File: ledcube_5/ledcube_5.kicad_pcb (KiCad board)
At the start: 2 copper layers, 60 parts, among them J1 Conn_01x05_MountingPin, Q1 PN2222A, Q2 PN2222A, Q3 PN2222A, Q4 PN2222A, Q5 PN2222A, U1 74HC595, U2 74HC595, U3 74HC595, U4 74HC595

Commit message: ledcube pcb tracks
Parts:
- added J2: Conn_01x01, Connector_Pin:Pin_D1.0mm_L10.0mm, F.Cu at (241.3, 102.9)
- added J3: Conn_01x01, Connector_Pin:Pin_D1.0mm_L10.0mm, F.Cu at (241.3, 106.9)
- added J4: Conn_01x01, Connector_Pin:Pin_D1.0mm_L10.0mm, F.Cu at (245.3, 102.9)
- added J5: Conn_01x01, Connector_Pin:Pin_D1.0mm_L10.0mm, F.Cu at (245.3, 106.9)
- added J6: Conn_01x01, Connector_Pin:Pin_D1.0mm_L10.0mm, F.Cu at (249.4, 102.9)
- J1: footprint Connector_PinHeader_1.00mm:PinHeader_1x05_P1.00mm_Vertical -> Connector_PinHeader_2.54mm:PinHeader_1x05_P2.54mm_Vertical
- moved J1 2.34 mm to (248.7, 82.0)
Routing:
- net GND: track 0.00 -> 231.7 mm
- net +5V: track 0.00 -> 210.6 mm
- net /U3_F: track 0.00 -> 104.6 mm
- net /A0: track 0.00 -> 84.8 mm
- net /A4: track 0.00 -> 84.6 mm
- net /U3_G: track 0.00 -> 80.7 mm
- net /U3_H: track 0.00 -> 69.0 mm
- net /U4_B: track 0.00 -> 67.1 mm
- net Net-(J6-Pad1): track 0.00 -> 58.3 mm
- net /U2_F: track 0.00 -> 57.5 mm
- net /U1_A: track 0.00 -> 57.3 mm
- net /U1_D: track 0.00 -> 52.4 mm
- net /U1_C: track 0.00 -> 49.2 mm
- net /U4_E: track 0.00 -> 45.3 mm
- net Net-(J5-Pad1): track 0.00 -> 44.1 mm
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
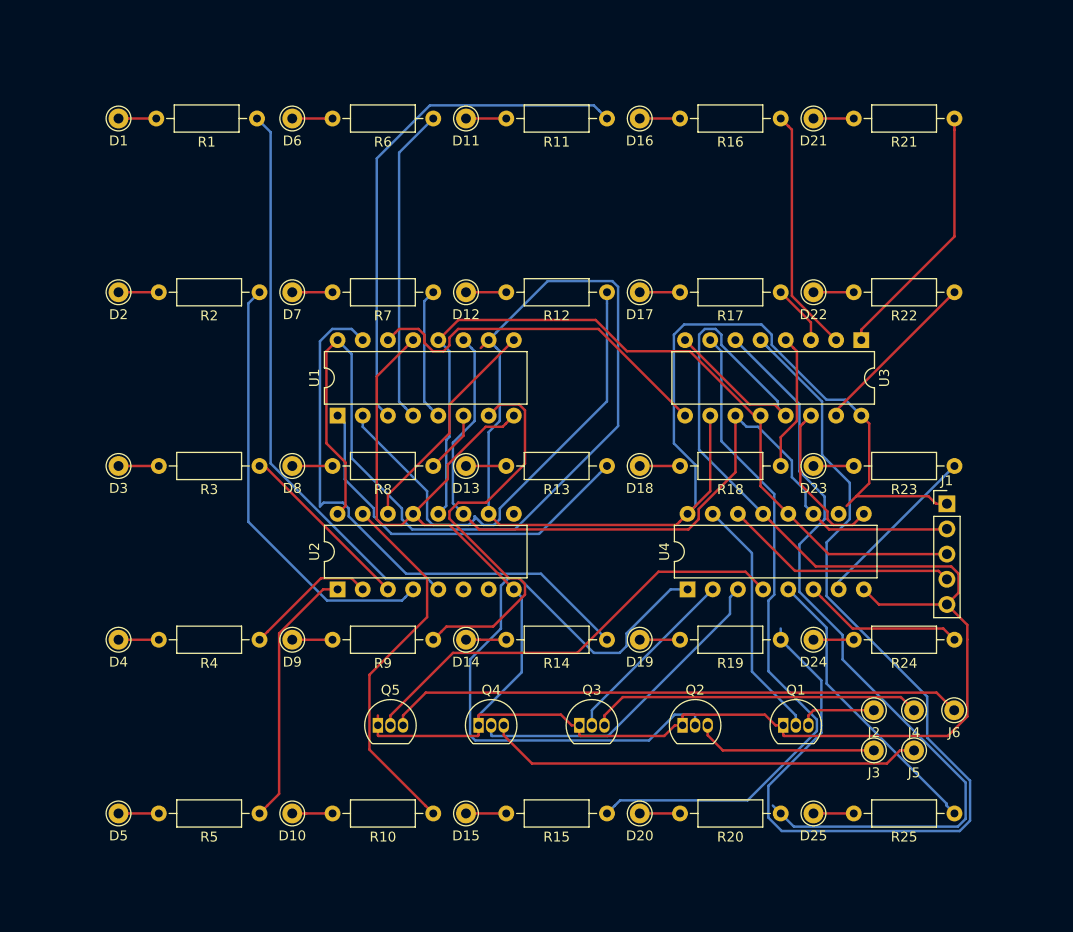
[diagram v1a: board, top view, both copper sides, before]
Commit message: fix missing R for transistors
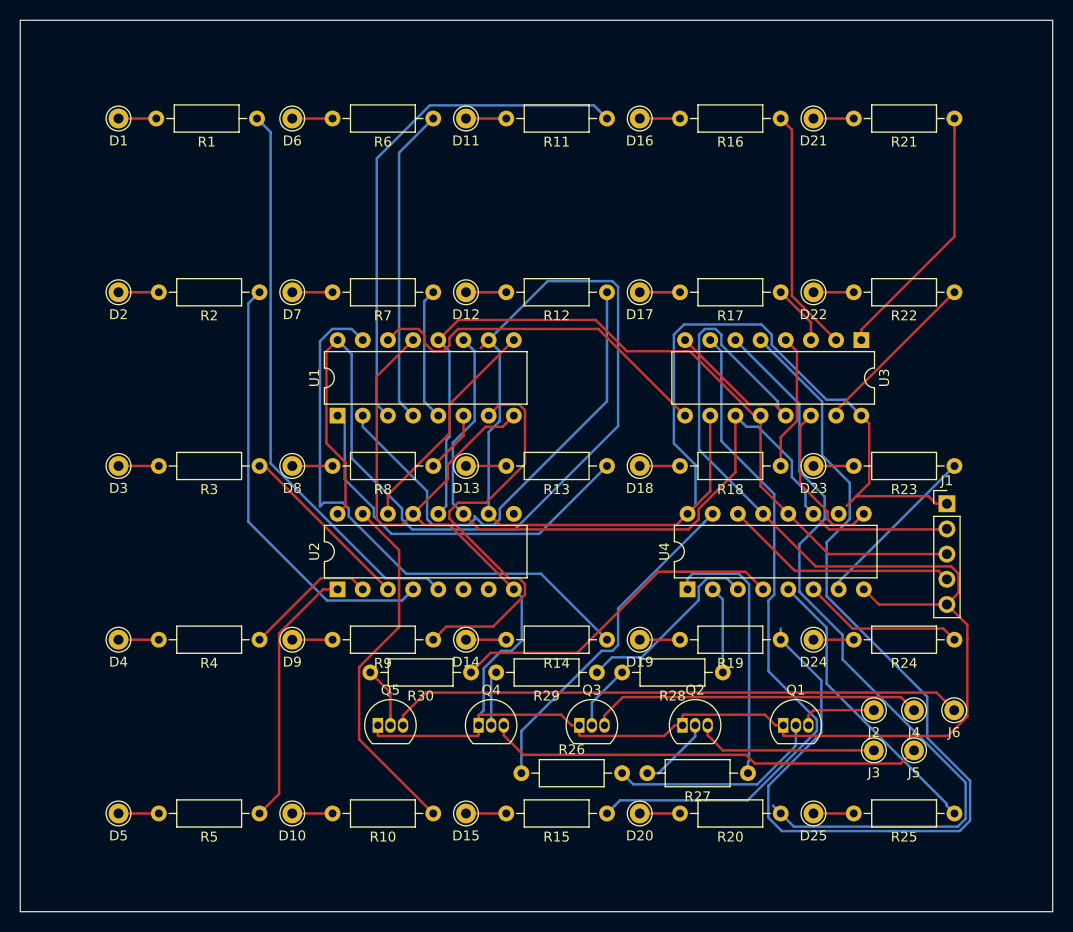
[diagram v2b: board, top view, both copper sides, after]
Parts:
- added R26: 510, Resistor_THT:R_Axial_DIN0207_L6.3mm_D2.5mm_P10.16mm_Horizontal, F.Cu at (205.7, 109.2)
- added R27: 510, Resistor_THT:R_Axial_DIN0207_L6.3mm_D2.5mm_P10.16mm_Horizontal, F.Cu at (228.6, 109.2)
- added R28: 510, Resistor_THT:R_Axial_DIN0207_L6.3mm_D2.5mm_P10.16mm_Horizontal, F.Cu at (226.1, 99.1)
- added R29: 510, Resistor_THT:R_Axial_DIN0207_L6.3mm_D2.5mm_P10.16mm_Horizontal, F.Cu at (213.4, 99.1)
- added R30: 510, Resistor_THT:R_Axial_DIN0207_L6.3mm_D2.5mm_P10.16mm_Horizontal, F.Cu at (200.7, 99.1)
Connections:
- Q1 pad 2: /U4_A -> Net-(Q1-Pad2)
- Q2 pad 2: /U4_B -> Net-(Q2-Pad2)
- Q3 pad 2: /U4_C -> Net-(Q3-Pad2)
- Q4 pad 2: /U4_D -> Net-(Q4-Pad2)
- Q5 pad 2: /U4_E -> Net-(Q5-Pad2)
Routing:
- net /U4_B: track 67.1 -> 27.0 mm
- net Net-(Q1-Pad2): track 0.00 -> 22.4 mm
- net /U4_D: track 33.0 -> 19.4 mm
- net /U4_E: track 45.3 -> 34.4 mm
- net /U4_C: track 18.8 -> 8.80 mm
- net /U4_A: track 25.2 -> 34.8 mm
- net Net-(Q2-Pad2): track 0.00 -> 7.49 mm
- net Net-(Q5-Pad2): track 0.00 -> 7.18 mm
- net Net-(Q3-Pad2): track 0.00 -> 6.60 mm
- net Net-(Q4-Pad2): track 0.00 -> 5.54 mm
- net /U2_A: track 38.0 -> 36.5 mm
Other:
- board outline added: 104.1 x 89.9 mm

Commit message: ledcube mounting holes and silkscreen
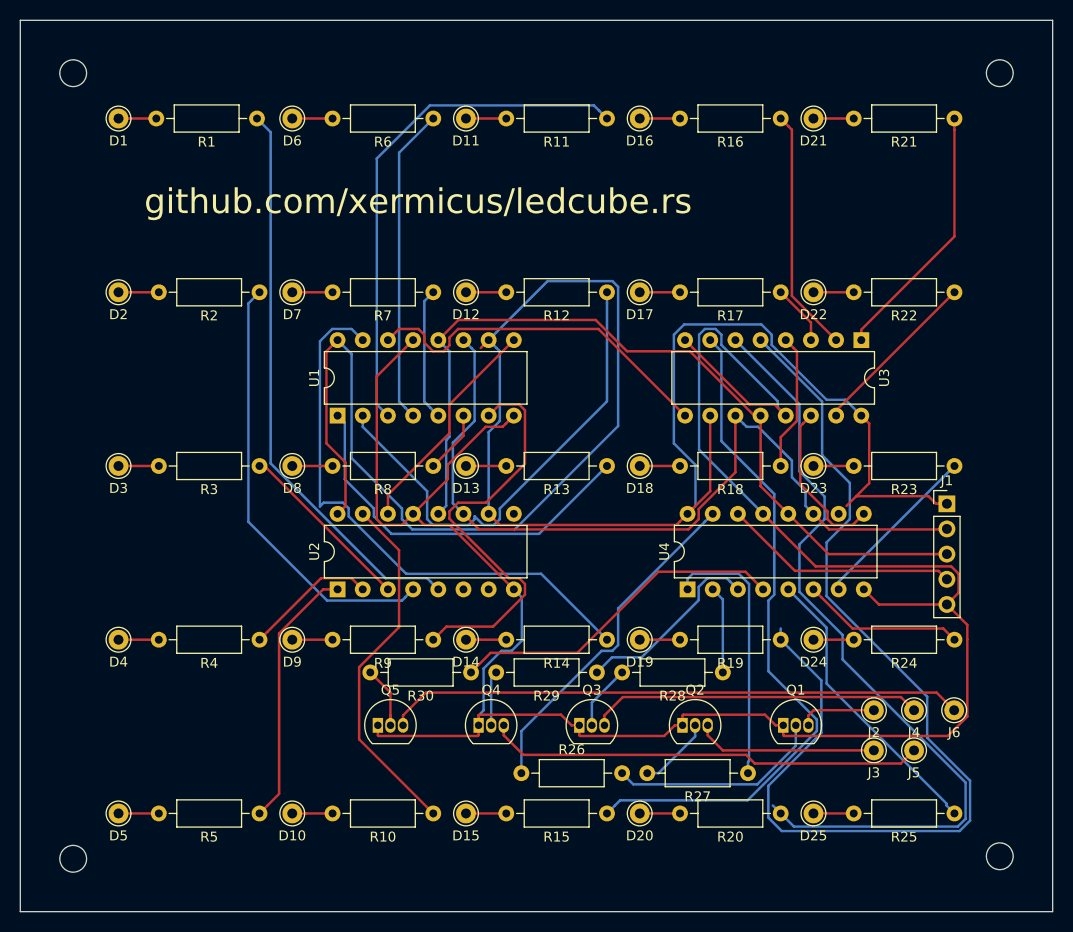
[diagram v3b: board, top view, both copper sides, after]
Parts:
- added REF**: MountingHole_2.7mm_M2.5, MountingHole:MountingHole_2.7mm_M2.5, F.Cu at (254.0, 117.6)
- added REF**: MountingHole_2.7mm_M2.5, MountingHole:MountingHole_2.7mm_M2.5, F.Cu at (160.5, 117.9)
- added REF**: MountingHole_2.7mm_M2.5, MountingHole:MountingHole_2.7mm_M2.5, F.Cu at (160.5, 38.6)
- added REF**: MountingHole_2.7mm_M2.5, MountingHole:MountingHole_2.7mm_M2.5, F.Cu at (254.0, 38.6)
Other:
- board text added: "github.com/xermicus/ledcube.rs"
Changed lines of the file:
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@@
   (general
     (thickness 1.6)
-    (drawings 8)
+    (drawings 9)
     (tracks 454)
     (zones 0)
-    (modules 70)
+    (modules 74)
     (nets 77)
   )
@@
     (add_net "Net-(U2-Pad9)")
   )
+  (module MountingHole:MountingHole_2.7mm_M2.5 (layer F.Cu)
+    (at 254 117.602)
+    (descr "Mounting Hole 2.7mm, no annular, M2.5")
+    (tags "mounting hole 2.7mm no annular m2.5")
+    (attr virtual)
+    (fp_text reference REF** (at 0 -3.7) (layer F.SilkS) hide
+      (effects (font (size 1 1) (thickness 0.15)))
+    )
+    (fp_text value MountingHole_2.7mm_M2.5 (at 0 3.7) (layer F.Fab)
+      (effects (font (size 1 1) (thickness 0.15)))
+    )
+    (fp_circle (center 0 0) (end 2.95 0) (layer F.CrtYd) (width 0.05))
+    (fp_circle (center 0 0) (end 2.7 0) (layer Cmts.User) (width 0.15))
+    (fp_text user %R (at 0.3 0) (layer F.Fab)
+      (effects (font (size 1 1) (thickness 0.15)))
+    )
+    (pad 1 np_thru_hole circle (at 0 0) (size 2.7 2.7) (drill 2.7) (layers *.Cu *.Mask))
+  )
+  (module MountingHole:MountingHole_2.7mm_M2.5 (layer F.Cu)
+    (at 160.528 117.856)
+    (descr "Mounting Hole 2.7mm, no annular, M2.5")
+    (tags "mounting hole 2.7mm no annular m2.5")
+    (attr virtual)
+    (fp_text reference REF** (at 0 -3.7) (layer F.SilkS) hide
+      (effects (font (size 1 1) (thickness 0.15)))
+    )
+    (fp_text value MountingHole_2.7mm_M2.5 (at 0 3.7) (layer F.Fab)
+      (effects (font (size 1 1) (thickness 0.15)))
+    )
+    (fp_circle (center 0 0) (end 2.95 0) (layer F.CrtYd) (width 0.05))
+    (fp_circle (center 0 0) (end 2.7 0) (layer Cmts.User) (width 0.15))
+    (fp_text user %R (at 0.3 0) (layer F.Fab)
+      (effects (font (size 1 1) (thickness 0.15)))
+    )
+    (pad 1 np_thru_hole circle (at 0 0) (size 2.7 2.7) (drill 2.7) (layers *.Cu *.Mask))
+  )
+  (module MountingHole:MountingHole_2.7mm_M2.5 (layer F.Cu)
+    (at 160.528 38.608)
+    (descr "Mounting Hole 2.7mm, no annular, M2.5")
+    (tags "mounting hole 2.7mm no annular m2.5")
+    (attr virtual)
+    (fp_text reference REF** (at 0 -3.7) (layer F.SilkS) hide
+      (effects (font (size 1 1) (thickness 0.15)))
+    )
+    (fp_text value MountingHole_2.7mm_M2.5 (at 0 3.7) (layer F.Fab)
+      (effects (font (size 1 1) (thickness 0.15)))
+    )
+    (fp_circle (center 0 0) (end 2.95 0) (layer F.CrtYd) (width 0.05))
+    (fp_circle (center 0 0) (end 2.7 0) (layer Cmts.User) (width 0.15))
+    (fp_text user %R (at 0.3 0) (layer F.Fab)
+      (effects (font (size 1 1) (thickness 0.15)))
+    )
+    (pad 1 np_thru_hole circle (at 0 0) (size 2.7 2.7) (drill 2.7) (layers *.Cu *.Mask))
+  )
+  (module MountingHole:MountingHole_2.7mm_M2.5 (layer F.Cu)
+    (at 254 38.608)
+    (descr "Mounting Hole 2.7mm, no annular, M2.5")
+    (tags "mounting hole 2.7mm no annular m2.5")
+    (attr virtual)
+    (fp_text reference REF** (at 0 -3.7) (layer F.SilkS) hide
+      (effects (font (size 1 1) (thickness 0.15)))
+    )
+    (fp_text value MountingHole_2.7mm_M2.5 (at 0 3.7) (layer F.Fab)
+      (effects (font (size 1 1) (thickness 0.15)))
+    )
+    (fp_circle (center 0 0) (end 2.95 0) (layer F.CrtYd) (width 0.05))
+    (fp_circle (center 0 0) (end 2.7 0) (layer Cmts.User) (width 0.15))
+    (fp_text user %R (at 0.3 0) (layer F.Fab)
+      (effects (font (size 1 1) (thickness 0.15)))
+    )
+    (pad 1 np_thru_hole circle (at 0 0) (size 2.7 2.7) (drill 2.7) (layers *.Cu *.Mask))
+  )
   (module Resistor_THT:R_Axial_DIN0207_L6.3mm_D2.5mm_P10.16mm_Horizontal (layer F.Cu)
     (at 200.66 99.06 180)
@@
     )
   )
+  (gr_text github.com/xermicus/ledcube.rs (at 195.326 51.562) (layer F.SilkS)
+    (effects (font (size 2.5 2.5) (thickness 0.25)))
+  )
   (gr_line (start 259.334 33.274) (end 259.334 123.19) (layer Edge.Cuts) (width 0.1))
